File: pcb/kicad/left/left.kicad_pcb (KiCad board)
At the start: 2 copper layers, 135.9 x 89.9 mm, 61 parts, among them J1 USB_C_Receptacle_USB2.0, J2 AudioJack4, J3 Conn_01x12_Male, SW1 BOOT, SW10 SW_Push, SW12 SW_Push, SW13 SW_Push, SW14 SW_Push, SW15 SW_Push, SW17 SW_Push, SW18 SW_Push, SW19 SW_Push, SW2 RESET, SW21 SW_Push, SW22 SW_Push, SW23 SW_Push, SW24 SW_Push, SW3 SW_Push, SW31 SW_Push, SW32 SW_Push, SW33 SW_Push, SW34 SW_Push, SW4 SW_Push, SW5 SW_Push, SW7 SW_Push, SW8 SW_Push, SW9 SW_Push, U1 STM32, U2 LDO

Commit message: right advances
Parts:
- J3: footprint kicad-usb:Harwin_M20-89012xx_1x12_P2.54mm_Horizontal -> kicad-harwin:Harwin_M20-89012xx_1x12_P2.54mm_Horizontal
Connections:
- U1 pad 25: Net-(U1-Pad25) -> GND
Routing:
- net GND: track 18.2 -> 19.6 mm

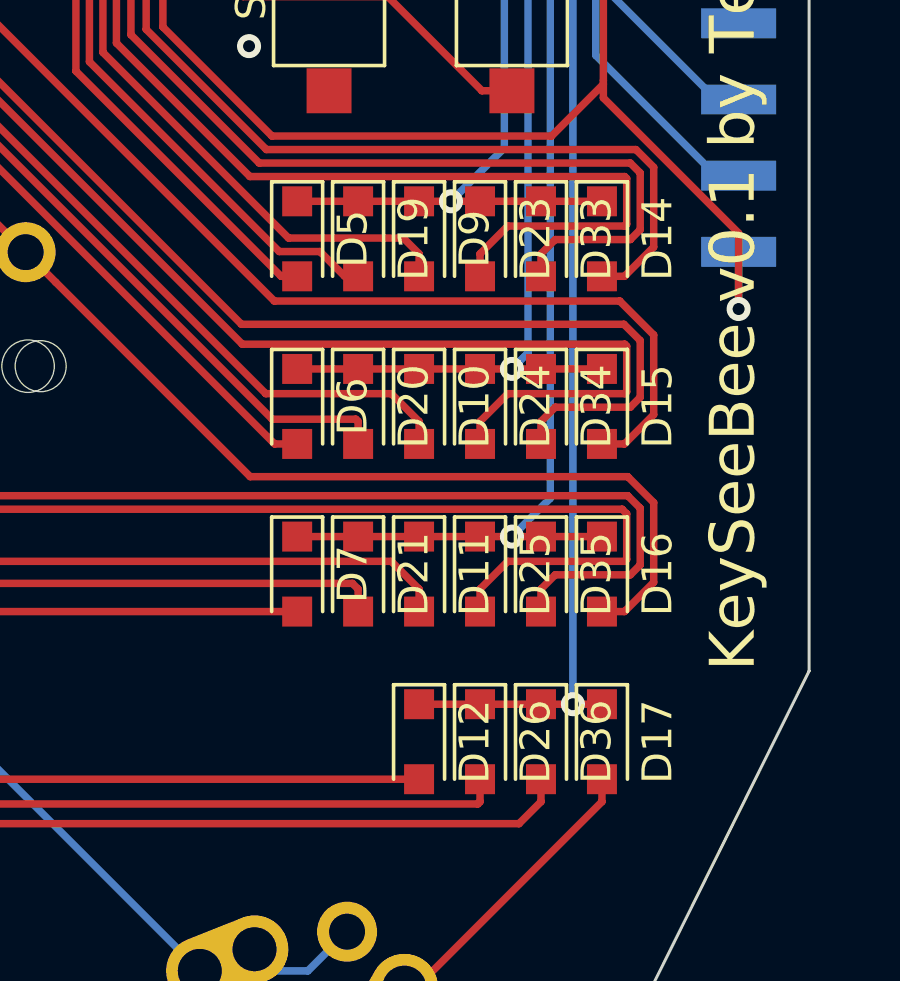
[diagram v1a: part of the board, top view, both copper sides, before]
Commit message: left: correct diode bug
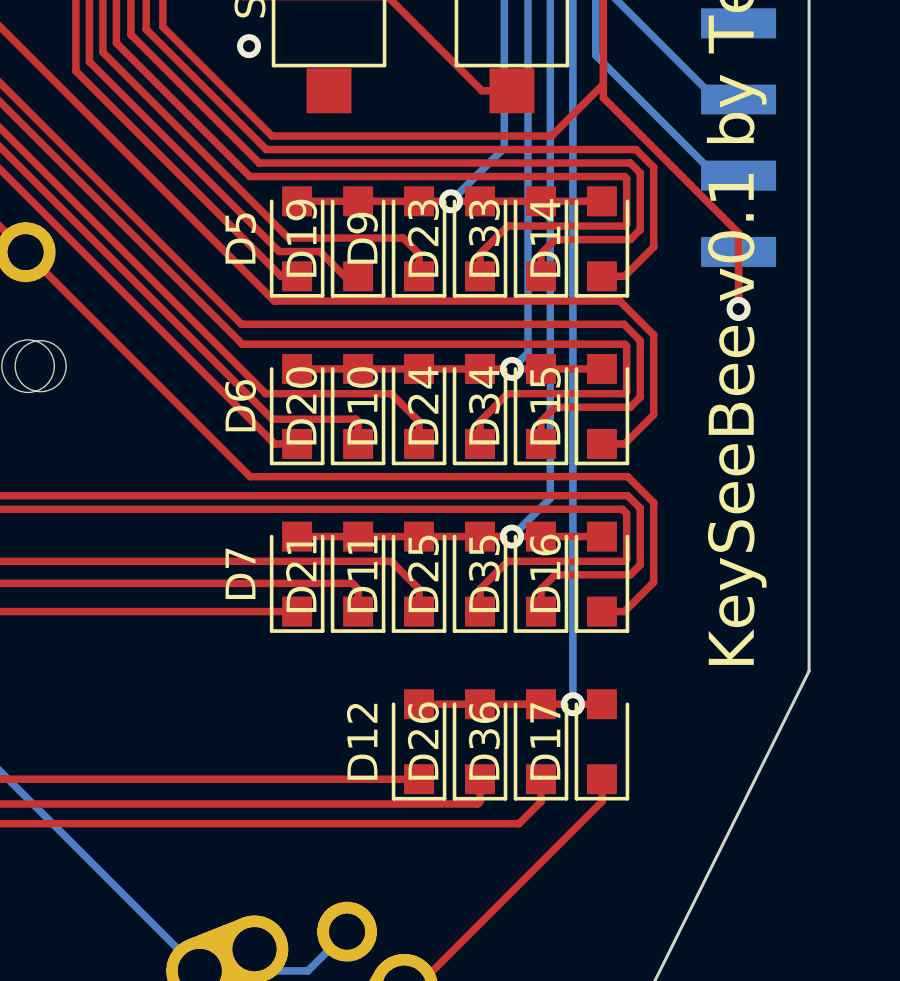
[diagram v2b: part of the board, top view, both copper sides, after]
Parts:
- J2: footprint Keebio:TRRS-PJ-320A-no-Fmask -> keebio:TRRS-PJ-320A-no-Fmask
- turned D10 to 90 degrees
- turned D11 to 90 degrees
- turned D12 to 90 degrees
- turned D14 to 90 degrees
- turned D15 to 90 degrees
- turned D16 to 90 degrees
- turned D17 to 90 degrees
- turned D19 to 90 degrees
- turned D20 to 90 degrees
- turned D21 to 90 degrees
- turned D23 to 90 degrees
- turned D24 to 90 degrees
- turned D25 to 90 degrees
- turned D26 to 90 degrees
- turned D33 to 90 degrees
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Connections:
- D10 pad 1: ROW2 -> Net-(D10-Pad1)
- D10 pad 2: Net-(D10-Pad2) -> ROW2
- D11 pad 1: ROW3 -> Net-(D11-Pad1)
- D11 pad 2: Net-(D11-Pad2) -> ROW3
- D12 pad 1: ROW4 -> Net-(D12-Pad1)
- D12 pad 2: Net-(D12-Pad2) -> ROW4
- D14 pad 1: ROW1 -> Net-(D14-Pad1)
- D14 pad 2: Net-(D14-Pad2) -> ROW1
- D15 pad 1: ROW2 -> Net-(D15-Pad1)
- D15 pad 2: Net-(D15-Pad2) -> ROW2
- D16 pad 1: ROW3 -> Net-(D16-Pad1)
- D16 pad 2: Net-(D16-Pad2) -> ROW3
- D17 pad 1: ROW4 -> Net-(D17-Pad1)
- D17 pad 2: Net-(D17-Pad2) -> ROW4
- D19 pad 1: ROW1 -> Net-(D19-Pad1)
- D19 pad 2: Net-(D19-Pad2) -> ROW1
- D20 pad 1: ROW2 -> Net-(D20-Pad1)
- D20 pad 2: Net-(D20-Pad2) -> ROW2
- D21 pad 1: ROW3 -> Net-(D21-Pad1)
- D21 pad 2: Net-(D21-Pad2) -> ROW3
- D23 pad 1: ROW1 -> Net-(D23-Pad1)
- D23 pad 2: Net-(D23-Pad2) -> ROW1
- D24 pad 1: ROW2 -> Net-(D24-Pad1)
- D24 pad 2: Net-(D24-Pad2) -> ROW2
- D25 pad 1: ROW3 -> Net-(D25-Pad1)
- D25 pad 2: Net-(D25-Pad2) -> ROW3
- D26 pad 1: ROW4 -> Net-(D26-Pad1)
- D26 pad 2: Net-(D26-Pad2) -> ROW4
- D33 pad 1: ROW1 -> Net-(D33-Pad1)
- D33 pad 2: Net-(D33-Pad2) -> ROW1
- D34 pad 1: ROW2 -> Net-(D34-Pad1)
- D34 pad 2: Net-(D34-Pad2) -> ROW2
- D35 pad 1: ROW3 -> Net-(D35-Pad1)
- D35 pad 2: Net-(D35-Pad2) -> ROW3
- D36 pad 1: ROW4 -> Net-(D36-Pad1)
- D36 pad 2: Net-(D36-Pad2) -> ROW4
- D5 pad 1: ROW1 -> Net-(D5-Pad1)
- D5 pad 2: Net-(D5-Pad2) -> ROW1
- D6 pad 1: ROW2 -> Net-(D6-Pad1)
- D6 pad 2: Net-(D6-Pad2) -> ROW2
- D7 pad 1: ROW3 -> Net-(D7-Pad1)
- D7 pad 2: Net-(D7-Pad2) -> ROW3
- D9 pad 1: ROW1 -> Net-(D9-Pad1)
- D9 pad 2: Net-(D9-Pad2) -> ROW1
- SW10 pad 1: Net-(D12-Pad2) -> Net-(D12-Pad1)
- SW12 pad 1: Net-(D14-Pad2) -> Net-(D14-Pad1)
- SW13 pad 1: Net-(D15-Pad2) -> Net-(D15-Pad1)
- SW14 pad 1: Net-(D16-Pad2) -> Net-(D16-Pad1)
- SW15 pad 1: Net-(D17-Pad2) -> Net-(D17-Pad1)
- SW17 pad 1: Net-(D19-Pad2) -> Net-(D19-Pad1)
- SW18 pad 1: Net-(D20-Pad2) -> Net-(D20-Pad1)
- SW19 pad 1: Net-(D21-Pad2) -> Net-(D21-Pad1)
- SW21 pad 1: Net-(D23-Pad2) -> Net-(D23-Pad1)
- SW22 pad 1: Net-(D24-Pad2) -> Net-(D24-Pad1)
- SW23 pad 1: Net-(D25-Pad2) -> Net-(D25-Pad1)
- SW24 pad 1: Net-(D26-Pad2) -> Net-(D26-Pad1)
- SW3 pad 1: Net-(D5-Pad2) -> Net-(D5-Pad1)
- SW31 pad 1: Net-(D33-Pad2) -> Net-(D33-Pad1)
- SW32 pad 1: Net-(D34-Pad2) -> Net-(D34-Pad1)
- SW33 pad 1: Net-(D35-Pad2) -> Net-(D35-Pad1)
- SW34 pad 1: Net-(D36-Pad2) -> Net-(D36-Pad1)
- SW4 pad 1: Net-(D6-Pad2) -> Net-(D6-Pad1)
- SW5 pad 1: Net-(D7-Pad2) -> Net-(D7-Pad1)
- SW7 pad 1: Net-(D9-Pad2) -> Net-(D9-Pad1)
- SW8 pad 1: Net-(D10-Pad2) -> Net-(D10-Pad1)
- SW9 pad 1: Net-(D11-Pad2) -> Net-(D11-Pad1)
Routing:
- net Net-(D5-Pad2): track 129.5 -> 0.00 mm
- net Net-(D5-Pad1): track 0.00 -> 129.5 mm
- net Net-(D6-Pad2): track 116.1 -> 0.00 mm
- net Net-(D6-Pad1): track 0.00 -> 116.1 mm
- net Net-(D19-Pad2): track 110.7 -> 0.00 mm
- net Net-(D19-Pad1): track 0.00 -> 110.7 mm
- net Net-(D7-Pad2): track 110.3 -> 0.00 mm
- net Net-(D7-Pad1): track 0.00 -> 110.3 mm
- net Net-(D9-Pad2): track 98.5 -> 0.00 mm
- net Net-(D9-Pad1): track 0.00 -> 98.5 mm
- net Net-(D20-Pad2): track 98.1 -> 0.00 mm
- net Net-(D20-Pad1): track 0.00 -> 98.1 mm
- net Net-(D23-Pad2): track 92.9 -> 0.00 mm
- net Net-(D23-Pad1): track 0.00 -> 92.9 mm
- net Net-(D21-Pad2): track 92.5 -> 0.00 mm
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
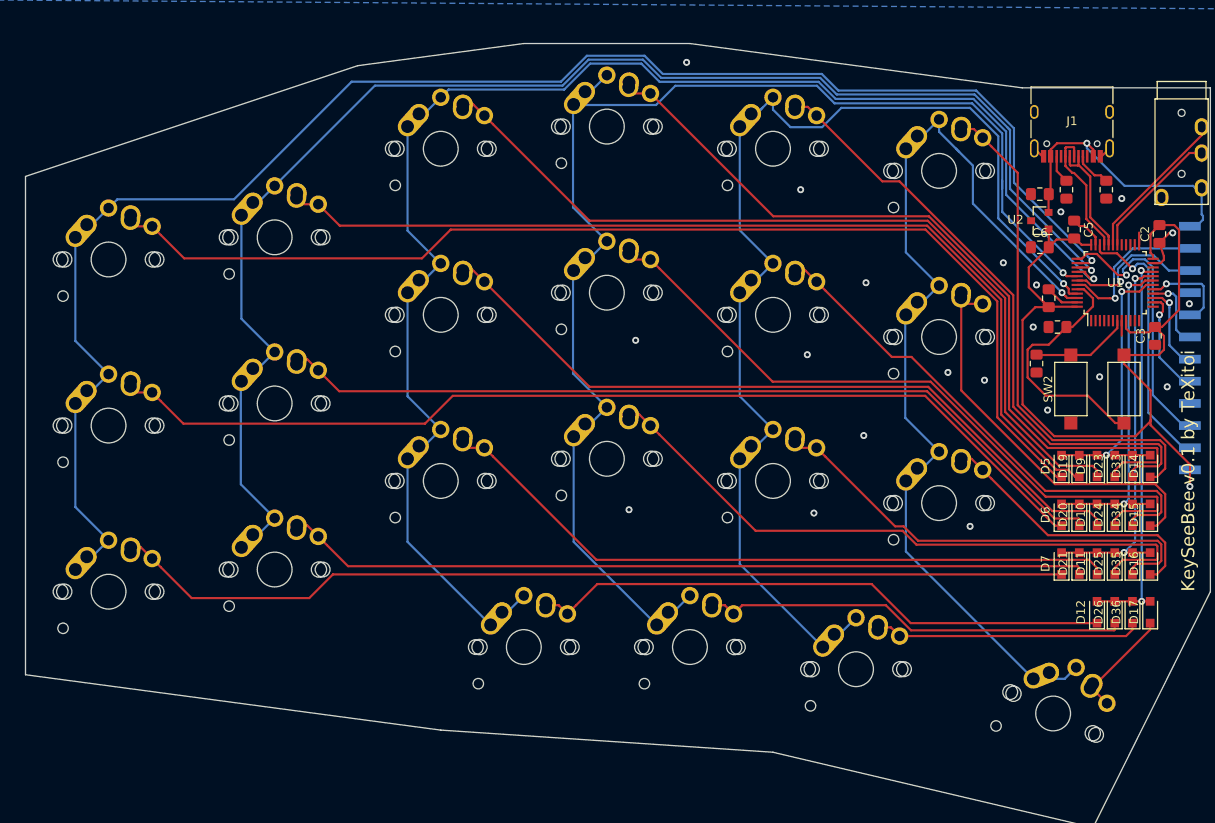
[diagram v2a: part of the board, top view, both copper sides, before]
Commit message: left: change switch footprint
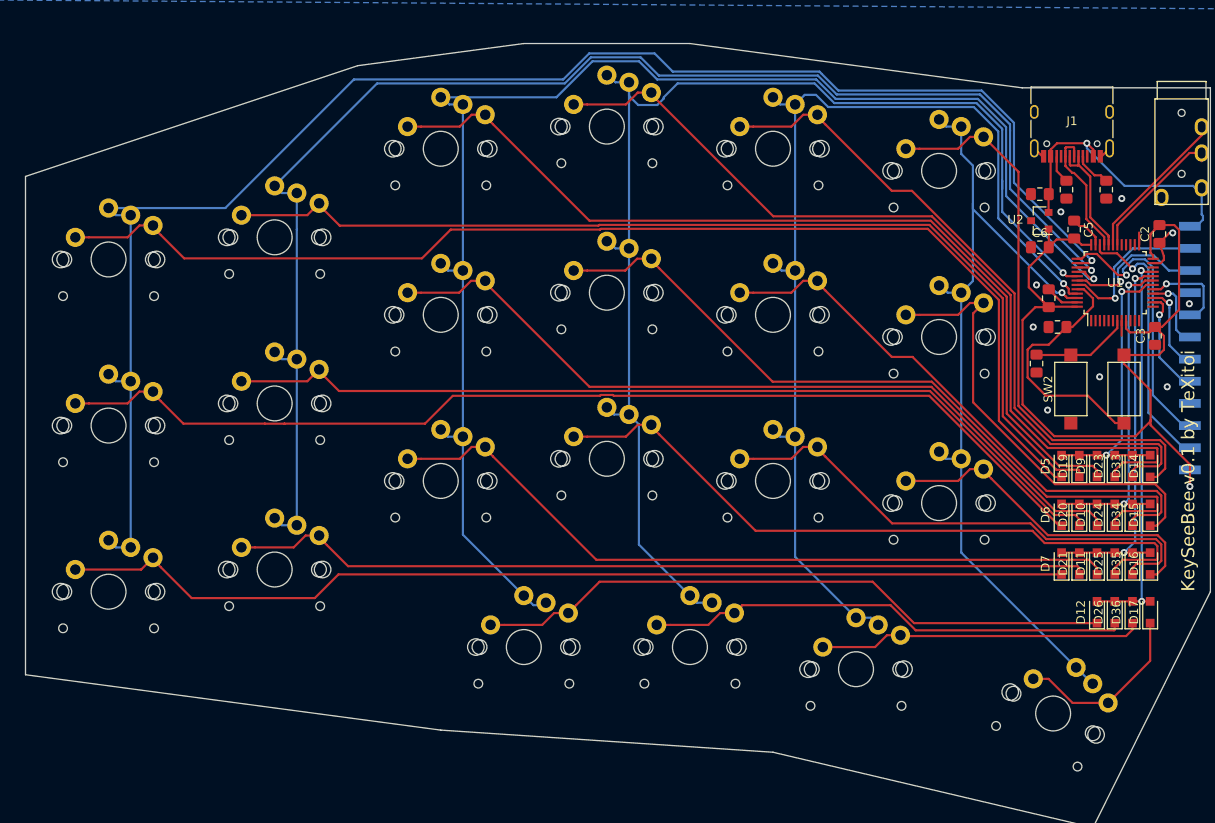
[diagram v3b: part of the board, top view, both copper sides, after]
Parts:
- SW10, SW12, SW13, SW14, SW15, SW17, SW18, SW19, SW21, SW22, SW23, SW24, SW3, SW31, SW32, SW33, SW34, SW4, SW5, SW7, SW8, SW9: footprint Keebio:MX-Alps-Choc-1U-NoLED -> foostan-kbd:CherryMX_Choc_1u
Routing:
- net COL5: track 138.2 -> 122.1 mm
- net COL6: track 112.6 -> 96.7 mm
- net COL4: track 154.9 -> 143.4 mm
- net Net-(D17-Pad1): track 13.1 -> 20.9 mm
- net Net-(D19-Pad1): track 110.7 -> 118.1 mm
- net Net-(D5-Pad1): track 129.5 -> 136.6 mm
- net Net-(D23-Pad1): track 92.9 -> 99.9 mm
- net COL3: track 171.7 -> 164.9 mm
- net Net-(D6-Pad1): track 116.1 -> 122.8 mm
- net Net-(D12-Pad1): track 67.0 -> 73.7 mm
- net Net-(D9-Pad1): track 98.5 -> 105.2 mm
- net Net-(D35-Pad1): track 53.2 -> 59.9 mm
- net Net-(D24-Pad1): track 79.8 -> 86.5 mm
- net Net-(D11-Pad1): track 79.5 -> 86.2 mm
- net Net-(D33-Pad1): track 72.1 -> 78.7 mm
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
